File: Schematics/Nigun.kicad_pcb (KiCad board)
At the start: 4 copper layers, 54 x 50.1 mm, 244 parts, among them J1 RF IN, J1 USB-MICRO-B, J2 RF OUT, M1 Mounting_hole, M2 Mounting_hole, M3 Mounting_hole, M4 Mounting_hole, P1 CONN_02X04, P2 CONN_SWD, T1 TC1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

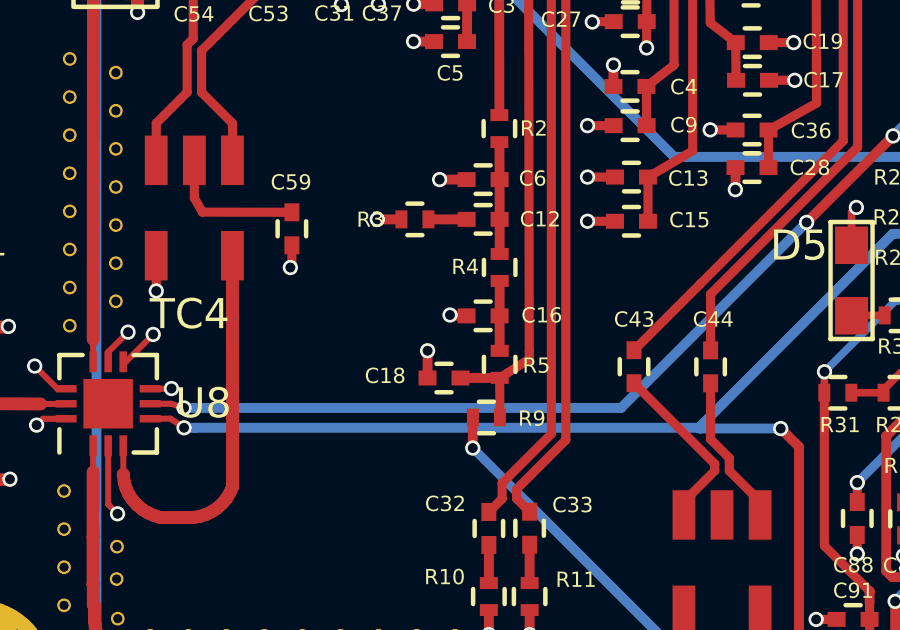
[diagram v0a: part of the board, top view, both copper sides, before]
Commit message: Switched order of VCC and GND layers
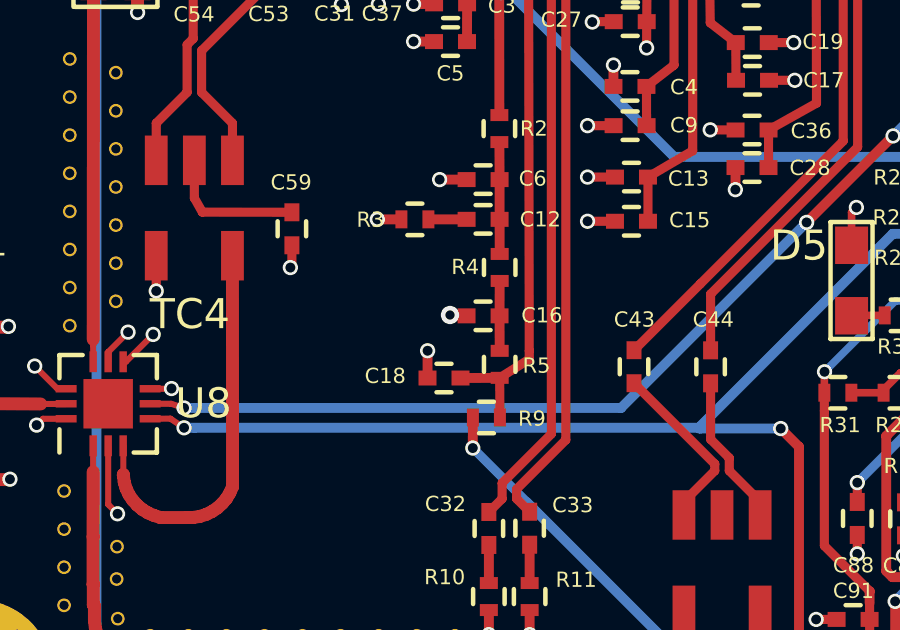
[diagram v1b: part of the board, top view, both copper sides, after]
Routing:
- net /VCC_3.3V: track 90.2 -> 90.8 mm
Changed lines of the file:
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@@
   (general
     (links 461)
-    (no_connects 5)
-    (area 106.070399 39.4205 172.071634 94.3724)
+    (no_connects 205)
+    (area 115.342999 42.899999 169.543401 93.191001)
     (thickness 1.6)
     (drawings 4)
@@
   (layers
     (0 Front signal)
-    (1 VCC power)
-    (2 GND power hide)
+    (1 GND signal hide)
+    (2 VCC signal)
     (31 Back signal)
     (33 F.Adhes user)
@@
     (39 F.Mask user)
     (40 Dwgs.User user hide)
-    (41 Cmts.User user hide)
-    (42 Eco1.User user hide)
-    (43 Eco2.User user hide)
+    (41 Cmts.User user)
+    (42 Eco1.User user)
+    (43 Eco2.User user)
     (44 Edge.Cuts user)
     (45 Margin user)
@@
   )
   (setup
-    (last_trace_width 0.3048)
+    (last_trace_width 0.1524)
     (user_trace_width 0.2032)
     (user_trace_width 0.2032)
@@
   (segment (start 135.35016 77.76464) (end 134.82574 77.76464) (width 0.3302) (layer Front) (net 4))
   (segment (start 134.82574 77.76464) (end 134.7978 77.7367) (width 0.3302) (layer Front) (net 4))
-  (via (at 134.7978 77.7367) (size 0.508) (drill 0.3302) (layers Front Back) (net 4))
+  (via (at 134.7978 77.7367) (size 0.6096) (drill 0.3048) (layers Front Back) (net 4))
   (segment (start 158.97164 88.6079) (end 158.973868 88.610128) (width 0.3302) (layer Front) (net 4))
   (via (at 145.1356 88.7603) (size 0.508) (drill 0.3302) (layers Front Back) (net 4))
@@
   (segment (start 138.2882 62.3042) (end 138.29284 62.87516) (width 0.3302) (layer Front) (net 14))
   (segment (start 136.45388 79.8322) (end 135.14832 79.83728) (width 0.3302) (layer Front) (net 14))
+  (segment (start 125.514421 80.187966) (end 127.19847 80.187966) (width 0.3048) (layer VCC) (net 15))
+  (segment (start 130.586101 76.800335) (end 130.586101 75.379959) (width 0.3048) (layer VCC) (net 15))
+  (segment (start 127.19847 80.187966) (end 130.586101 76.800335) (width 0.3048) (layer VCC) (net 15))
+  (segment (start 130.586101 75.379959) (end 138.553475 67.412585) (width 0.3048) (layer VCC) (net 15))
+  (segment (start 138.553475 67.412585) (end 139.795887 67.412585) (width 0.3048) (layer VCC) (net 15))
+  (segment (start 139.795887 67.412585) (end 140.070198 67.686896) (width 0.3048) (layer VCC) (net 15))
+  (segment (start 140.070198 67.686896) (end 159.564362 67.686896) (width 0.3048) (layer VCC) (net 15))
+  (segment (start 159.564362 67.686896) (end 160.601658 66.6496) (width 0.3048) (layer VCC) (net 15))
   (segment (start 152.480862 45.428075) (end 152.226863 45.174076) (width 0.3302) (layer VCC) (net 15))
   (segment (start 168.128436 61.075649) (end 152.480862 45.428075) (width 0.3302) (layer VCC) (net 15))
@@
   (segment (start 152.18968 46.19688) (end 152.18968 45.211259) (width 0.3302) (layer Front) (net 15))
   (via (at 152.226863 45.174076) (size 0.508) (drill 0.3302) (layers Front Back) (net 15))
-  (segment (start 125.514421 80.187966) (end 126.265776 80.187966) (width 0.3048) (layer VCC) (net 15))
-  (segment (start 139.795887 67.412585) (end 140.070198 67.686896) (width 0.3048) (layer VCC) (net 15))
-  (segment (start 140.070198 67.686896) (end 159.564362 67.686896) (width 0.3048) (layer VCC) (net 15))
-  (segment (start 126.265776 80.187966) (end 130.035301 76.418441) (width 0.3048) (layer VCC) (net 15))
-  (segment (start 130.035301 76.418441) (end 130.035301 75.930759) (width 0.3048) (layer VCC) (net 15))
-  (segment (start 130.035301 75.930759) (end 138.553475 67.412585) (width 0.3048) (layer VCC) (net 15))
-  (segment (start 138.553475 67.412585) (end 139.795887 67.412585) (width 0.3048) (layer VCC) (net 15))
-  (segment (start 159.564362 67.686896) (end 160.601658 66.6496) (width 0.3048) (layer VCC) (net 15))
   (segment (start 161.8361 66.6496) (end 161.8361 64.8716) (width 0.3302) (layer VCC) (net 15))
   (segment (start 161.8361 64.8716) (end 161.925 64.7827) (width 0.3302) (layer VCC) (net 15))
@@
     (polygon
       (pts
-        (xy 167.3479 43.434) (xy 116.967 43.3832) (xy 116.4844 92.1385) (xy 168.148 91.9734) (xy 168.1861 43.4213)
-        (xy 167.7543 43.4213) (xy 167.5638 43.434)
+        (xy 116.0653 43.6118) (xy 168.7322 43.6118) (xy 168.8465 92.6338) (xy 116.0272 92.6719) (xy 116.0145 43.6245)
+        (xy 116.0526 43.5991)
       )
     )

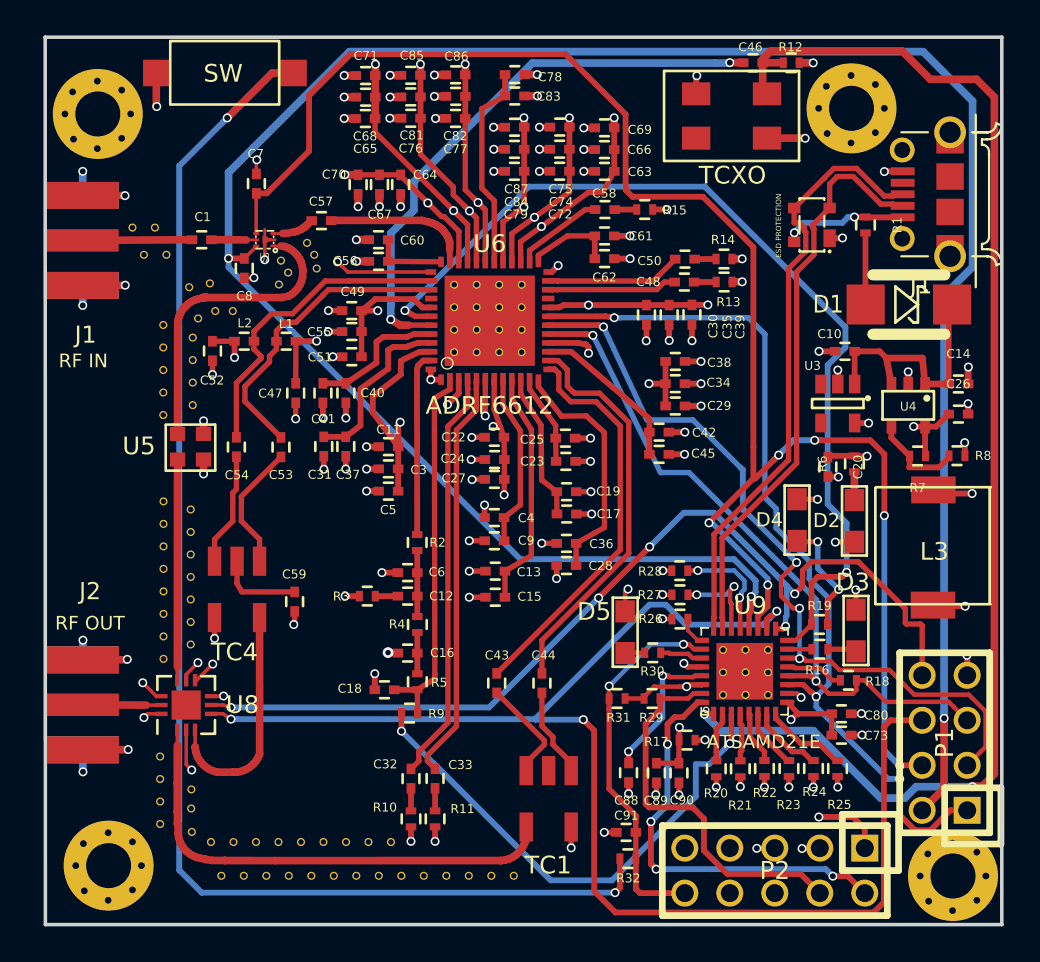
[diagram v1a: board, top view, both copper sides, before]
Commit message: Via size update and rearrange
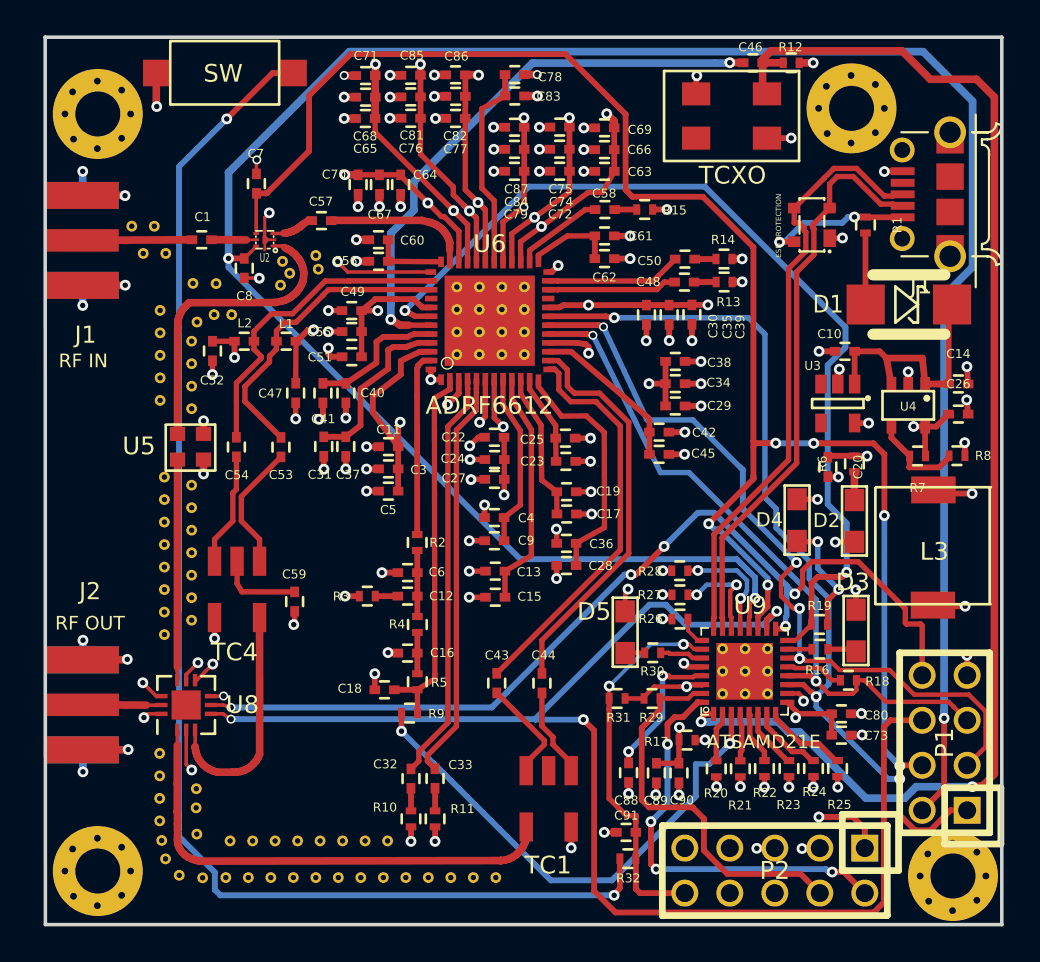
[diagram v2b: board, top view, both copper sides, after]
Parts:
- removed the REF** at (130.3, 53.2)
- removed the REF** at (124.9, 87.1)
- removed the REF** at (141.9, 89.0)
- added REF**: Via_10mil, Footprints:Via_drill12mil_pad24mil, F.Cu at (122.0, 88.3)
- added REF**: Via_10mil, Footprints:Via_drill12mil_pad24mil, F.Cu at (122.2, 89.4)
- added REF**: Via_10mil, Footprints:Via_drill12mil_pad24mil, F.Cu at (123.0, 90.3)
- added REF**: Via_10mil, Footprints:Via_drill12mil_pad24mil, F.Cu at (124.3, 90.4)
- REF** (x91): footprint Footprints:Via_drill12mil_pad18mil -> Footprints:Via_drill12mil_pad24mil
- moved REF** 1.58 mm to (123.7, 60.2)
- moved REF** 1.58 mm to (123.7, 61.4)
- moved REF** 1.58 mm to (123.7, 64.0)
- moved REF** 1.58 mm to (123.7, 62.7)
- moved REF** 1.58 mm to (124.0, 59.1)
- moved REF** 1.58 mm to (125.0, 58.7)
- moved REF** 1.58 mm to (126.0, 58.7)
- moved REF** 1.52 mm to (124.0, 88.0)
- moved REF** 1.50 mm to (140.0, 57.1)
- moved REF** 1.50 mm to (140.0, 59.6)
- moved REF** 1.50 mm to (138.7, 57.1)
- moved REF** 1.50 mm to (138.7, 59.6)
- moved REF** 1.50 mm to (141.2, 57.1)
- moved REF** 1.50 mm to (141.2, 59.6)
- moved REF** 1.50 mm to (142.5, 57.1)
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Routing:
- net Earth: track 135.3 -> 137.2 mm
- net Net-(D6-Pad4): track 7.02 -> 8.38 mm
- net /VCC_3.7V: track 202.3 -> 203.0 mm
- net IN_SW_VCTL2: track 95.0 -> 94.4 mm
- net /MCU_VDDIN: track 48.3 -> 48.9 mm
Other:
- net class Default: via_dia 0.508 -> 0.6096; via_drill 0.3302 -> 0.3048

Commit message: Finalized design for first prototype
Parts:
- removed the J1 at (115.5, 54.5)
- added G***: LOGO, Footprints:nigun_logo, F.Cu at (64.9, 48.0)
- added J3: RF_OUT, adafruit:SMA_EDGELAUNCH, F.Cu at (62.9, 61.5)
- added LOGO1: OSHW, hack-footprints:OSHW-LOGO, F.Cu at (77.6, 65.2)
- added REF**: Via_10mil, Footprints:Via_drill12mil_pad24mil, F.Cu at (63.5, 37.8)
- added REF**: Via_10mil, Footprints:Via_drill12mil_pad24mil, F.Cu at (65.1, 64.1)
- added REF**: Via_10mil, Footprints:Via_drill12mil_pad24mil, F.Cu at (66.3, 64.1)
- added REF**: Via_10mil, Footprints:Via_drill12mil_pad24mil, F.Cu at (66.4, 59.2)
- added REF**: Via_10mil, Footprints:Via_drill12mil_pad24mil, F.Cu at (64.9, 37.8)
- added REF**: Via_10mil, Footprints:Via_drill12mil_pad24mil, F.Cu at (66.2, 37.8)
- added REF**: Via_10mil, Footprints:Via_drill12mil_pad24mil, F.Cu at (63.7, 32.8)
- added REF**: Via_10mil, Footprints:Via_drill12mil_pad24mil, F.Cu at (64.9, 32.8)
- added REF**: Via_10mil, Footprints:Via_drill12mil_pad24mil, F.Cu at (66.2, 32.8)
- added REF**: Via_10mil, Footprints:Via_drill12mil_pad24mil, F.Cu at (63.7, 59.1)
- added REF**: Via_10mil, Footprints:Via_drill12mil_pad24mil, F.Cu at (65.1, 59.1)
- added REF**: Via_10mil, Footprints:Via_drill12mil_pad24mil, F.Cu at (63.8, 64.1)
- D6: value ESD PROTECTION -> D6
- J2: value RF OUT -> RF_IN; footprint Footprints:SMA_EDGELAUNCH -> adafruit:SMA_EDGELAUNCH
- L3: footprint SRR0603-100ML -> Footprints:SRR0603-100ML
- T1: value TC1 -> 43A+
- T2: value TC4 -> 1W+
- U6: footprint Footprints:ADRF6612 -> ADRF6612_LFCSP48:LFCSP48
- moved J2 69.6 mm to (62.8, 35.3)
- moved M3 56.6 mm to (113.5, 70.9)
- moved P1 56.5 mm to (113.4, 62.6)
- moved C8 56.3 mm to (73.7, 36.9)
- moved C10 56.1 mm to (107.9, 41.5)
- moved C24 56.1 mm to (88.1, 47.7)
- moved C25 56.1 mm to (92.1, 46.4)
- moved C28 56.1 mm to (92.2, 53.6)
- moved C3 56.1 mm to (82.1, 48.2)
- moved C35 56.1 mm to (98.0, 39.5)
- moved C36 56.1 mm to (92.2, 52.4)
- moved C39 56.1 mm to (99.2, 39.5)
- moved C40 56.1 mm to (79.7, 43.9)
- moved C43 56.1 mm to (88.2, 60.3)
- moved C47 56.1 mm to (76.9, 43.9)
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- renumbered SW to SW1, TCXO to U7
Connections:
- J2 pad P: Net-(J3-PadP) -> Net-(C1-Pad2)
- P1 pad 7: Earth -> TCXO_OUT
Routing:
- net Earth: track 137.2 -> 123.5 mm, vias 131 -> 122
- net TCXO_OUT: track 75.7 -> 79.6 mm
- net ADRF_CSNOT: track 50.4 -> 48.4 mm
- net IN_SW_VCTL2: track 94.4 -> 92.4 mm, vias 6 -> 5
- net OUT_SW_V2: track 55.6 -> 53.8 mm
- net IN_SW_VCTL1: track 134.4 -> 132.8 mm, vias 3 -> 2
- net Net-(D6-Pad4): track 8.38 -> 9.81 mm
- net /VCC_3.7V: track 203.0 -> 204.2 mm
- net USB_D+: track 34.1 -> 35.2 mm
- net USB_D-: track 32.7 -> 33.8 mm
- net ADRF_SCLK: track 44.4 -> 43.6 mm
- net ADRF_SDIO: track 39.7 -> 40.4 mm
- net OUT_SW_V1: track 78.8 -> 78.2 mm, vias 3 -> 4
- net ADRF_MUXOUT: track 53.7 -> 53.2 mm
